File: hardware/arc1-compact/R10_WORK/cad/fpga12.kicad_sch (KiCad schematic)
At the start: 77 parts, among them J10 12F JTAG, U31 LFE5U-12F-6TG144C, U32 iso SCK, U33 iso MOSI, U34 iso SS, U35 iso MISO, X3 25MHz

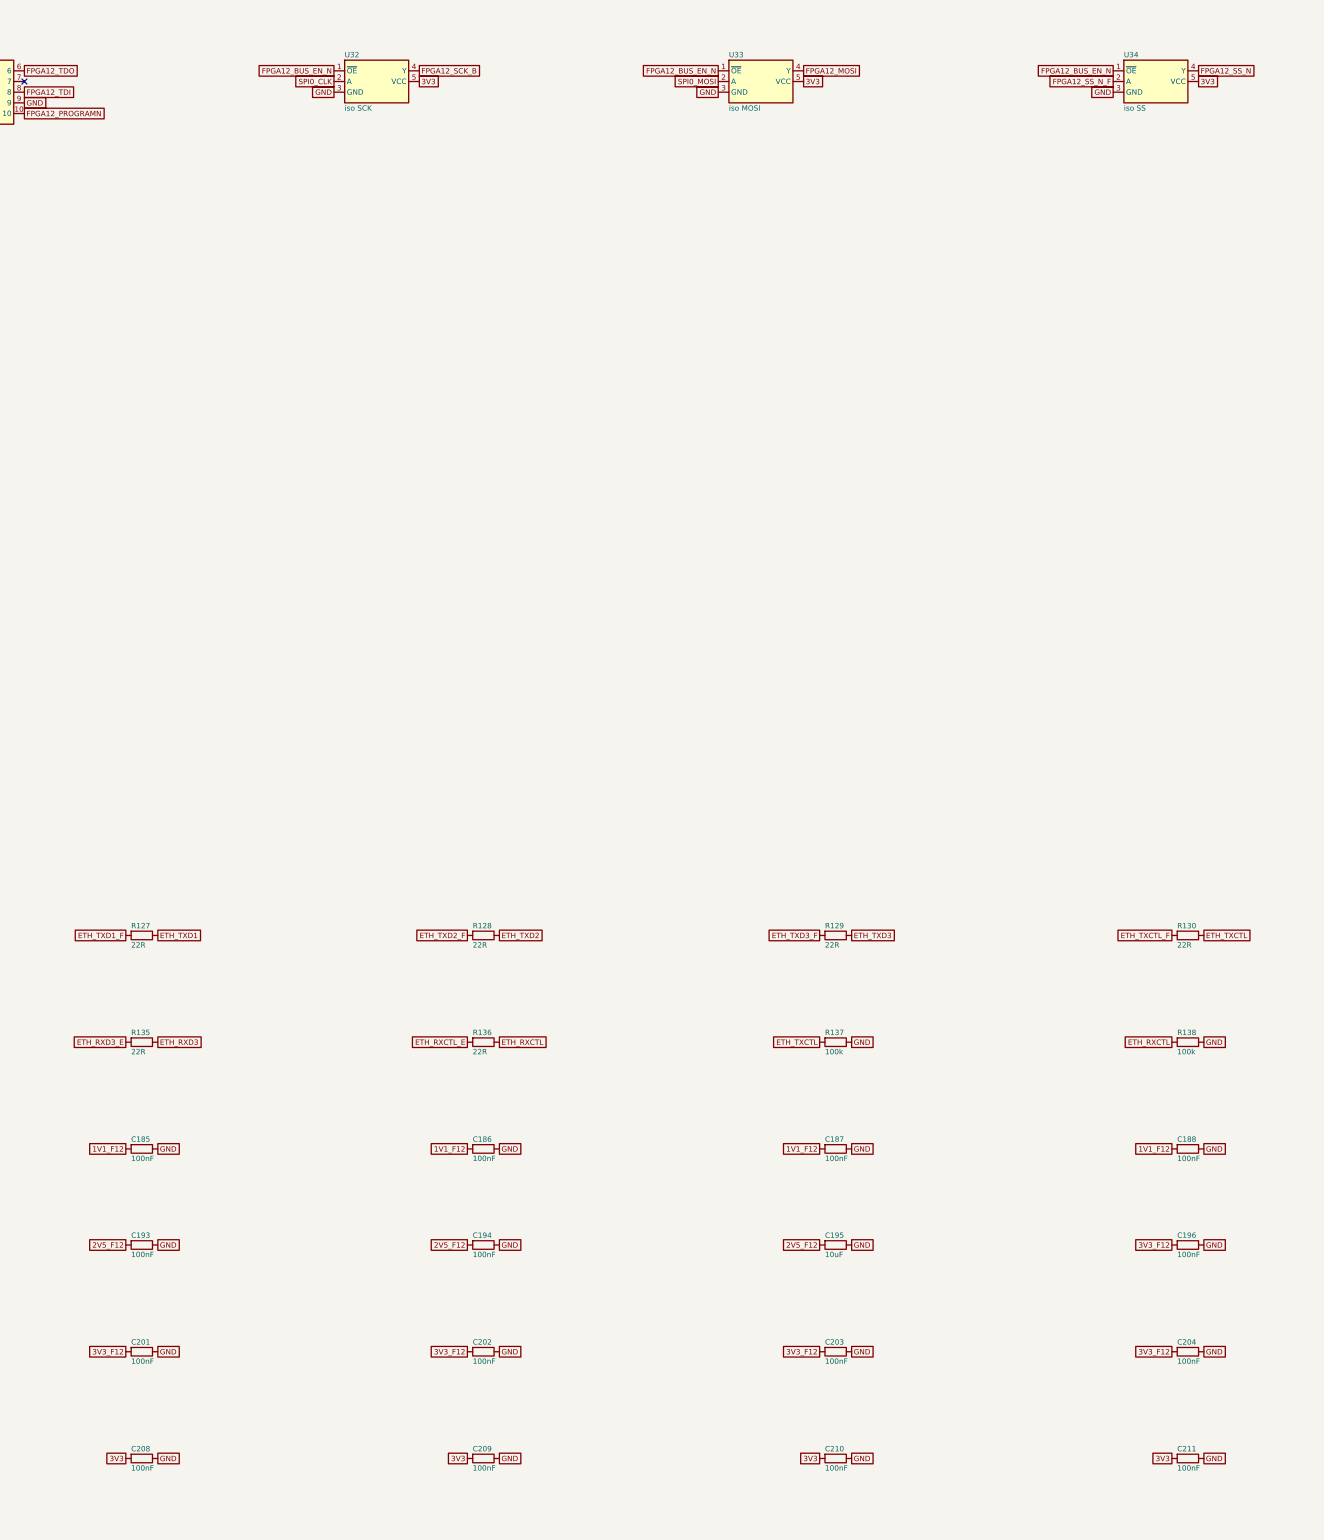
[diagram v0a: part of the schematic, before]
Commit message: R10 schematic: SDRAM net rename (collision with microSD clock found by crosscheck), 12F config buffers on 3V3_F12, crosscheck_r10 (A-H) PASS, every-pin review tables
Co-Authored-By: Claude Opus 5.5 <noreply@anthropic.com>
Claude-Session: https://claude.ai/code/session_01UkiuLdbjDvK75uDzAPKsGs
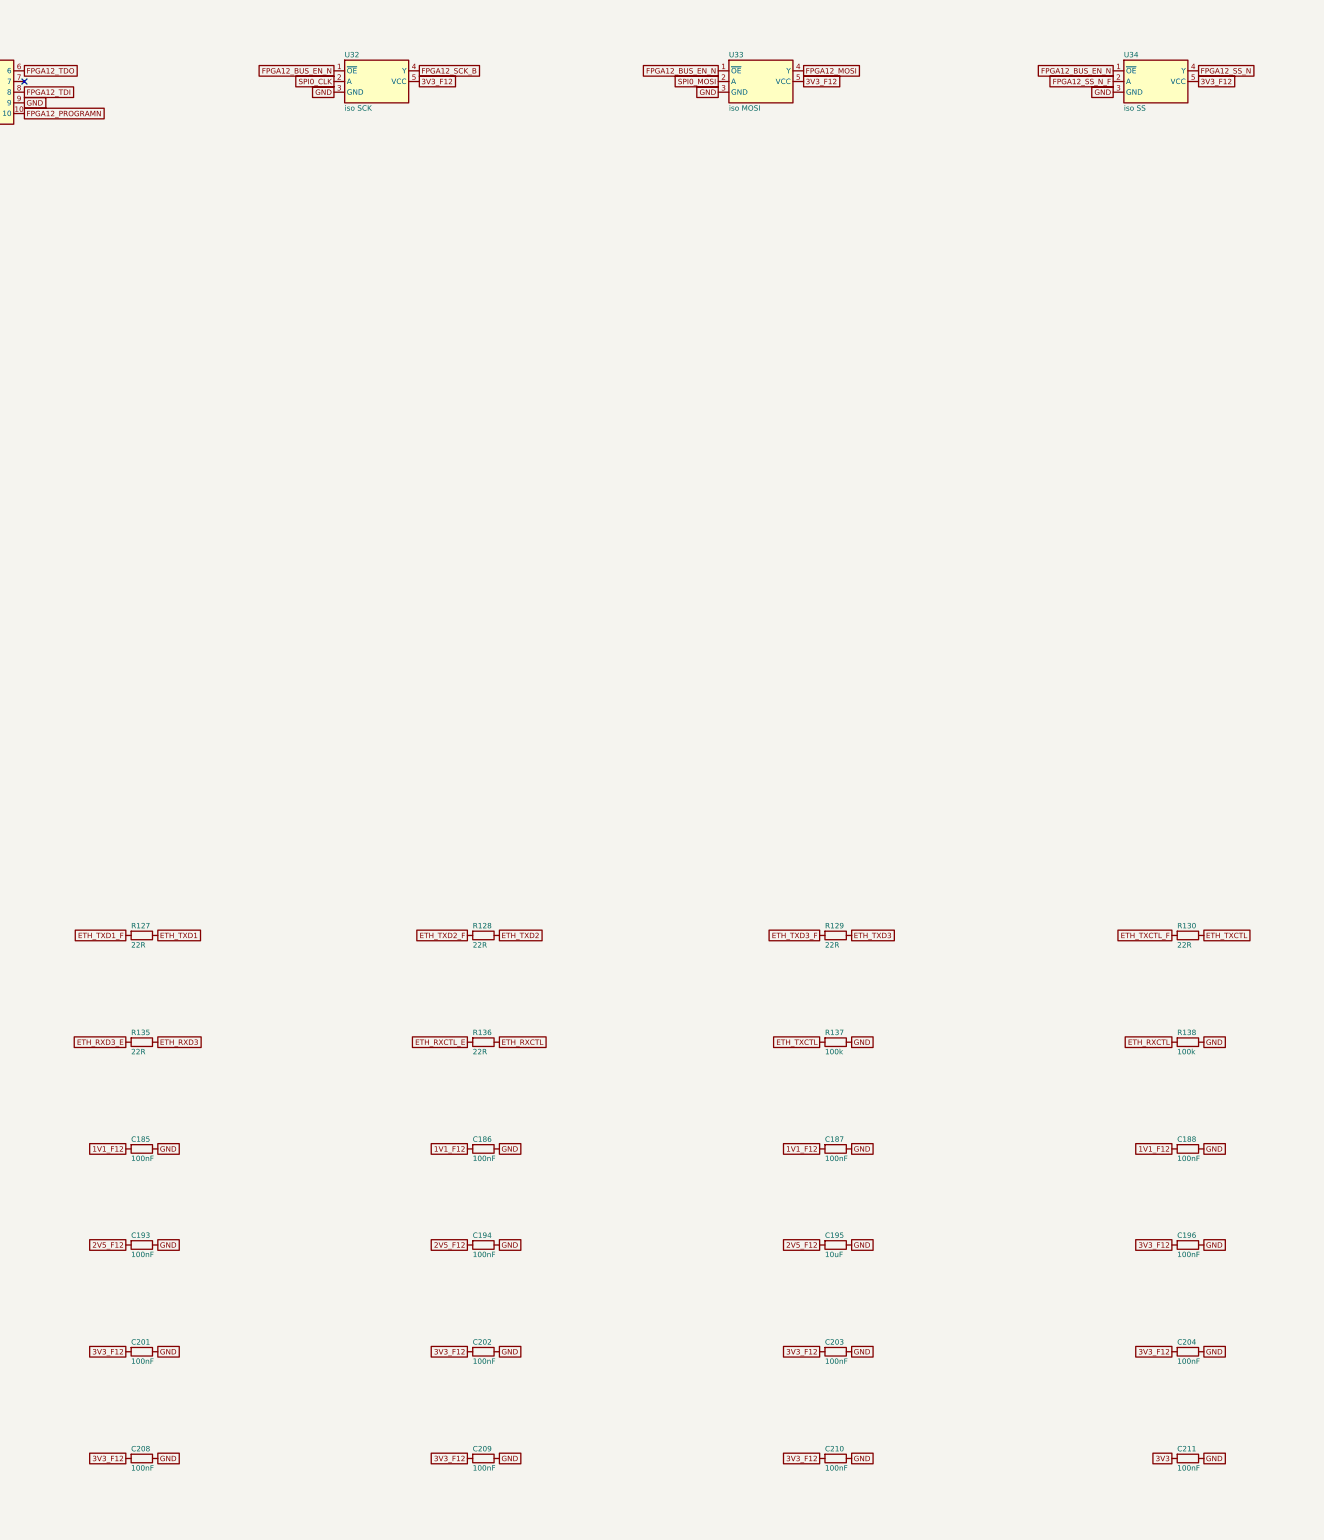
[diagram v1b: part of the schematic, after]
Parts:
- U32, U33, U34: Note (none) -> Ioff: powered with the FPGA it drives
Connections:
- net 3V3: no longer C208.1, C209.1, C210.1, U32.5 (VCC), U33.5 (VCC), U34.5 (VCC)
- net 3V3_F12: now also C208.1, C209.1, C210.1, U32.5 (VCC), U33.5 (VCC), U34.5 (VCC)

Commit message: R10 change order rev 1.1: HDMI audio (ADV7513), USB0 role mux + hub + 2x front USB-A, eMMC, buttonless board
Owner handoff ARC1_R10_Handoff rev 1.1 (spec/, SHA-256 recorded) implemented in the generated schematic:
- D8 ADV7513BSWZ replaces the TFP410 (supersedes D6): D213 RGB888 video, D213 I2C2 init,
  F133 I2S2 -> HDMI embedded audio; own 1.8 V buck + 3 filtered domains; R_EXT 887R.
  D[23:0] pin order verified from the datasheet glyph coordinates.
- D9 F133 USB0 -> TS3USB221A (default rear USB-C device/FEL) or USB2422 hub -> two
  TPS2051C-switched front USB-A ports; F133 USB1 remains the internal D213 link; the D213
  recovery USB-C becomes internal fixture pads.
- D10 Samsung KLMAG1JETD-B041 16 GB eMMC on F133 SMHC0 (CONDITIONAL: SMHC0 documented for SD).
- D11 no switches: fixture pad pairs; game buttons, microSD and speakers removed.
- crosscheck_r10 section I (handoff go/no-go: 4 exterior connectors, 0 switches, I2S wired
  to the HDMI transmitter, USB0/USB1 roles, eMMC wiring) PASS; ERC 0/0; pin review PASS.
Sources: ADV7513 DS Rev B (LCSC copy), ADI AN-1270, Linux adv7511 driver, USB2422
DS00001726A, TPS20xxC SLVSAU6I, Samsung eMMC DS (not committed: vendor-confidential mark).

Co-Authored-By: Claude Opus 5.5 <noreply@anthropic.com>
Claude-Session: https://claude.ai/code/session_01UkiuLdbjDvK75uDzAPKsGs
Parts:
- removed C183, C184, C185, C186, C187, C188, C191, C192, C193, C194, C196, C197, C198, C199, C200, C201, C202, C203, C204: 100nF, Capacitor_SMD:C_0402_1005Metric, symbol ARC1_R10:C0402
- removed C189, C190, C195: 10uF, Capacitor_SMD:C_0603_1608Metric, symbol ARC1_R10:C0603
- removed D5: 12F LED, LED_SMD:LED_0603_1608Metric, symbol ARC1_R10:LED
- removed J10: 12F JTAG, Connector_PinHeader_1.27mm:PinHeader_2x05_P1.27mm_Vertical_SMD, symbol ARC1_R10:HDR_2x5_127
- removed R125, R126, R127, R128, R129, R130: 22R, Resistor_SMD:R_0402_1005Metric, symbol ARC1_R10:R0402
- removed TP59: ETH_TXCK, TestPoint:TestPoint_Pad_D1.0mm, symbol ARC1_R10:TP
- removed TP60: ETH_RXCK, TestPoint:TestPoint_Pad_D1.0mm, symbol ARC1_R10:TP
- removed TP61: FPGA12_DONE, TestPoint:TestPoint_Pad_D1.0mm, symbol ARC1_R10:TP
- removed TP62: FPGA12_PROGRAMN, TestPoint:TestPoint_Pad_D1.0mm, symbol ARC1_R10:TP
- removed TP63: FPGA12_INITN, TestPoint:TestPoint_Pad_D1.0mm, symbol ARC1_R10:TP
- removed TP64: FPGA12_SCK, TestPoint:TestPoint_Pad_D1.0mm, symbol ARC1_R10:TP
- removed U31: LFE5U-12F-6TG144C, Package_QFP:TQFP-144_20x20mm_P0.5mm, symbol ARC1_R10:ECP5_12F_TQ144
- removed U32: iso SCK, Package_TO_SOT_SMD:SOT-353_SC-70-5, symbol ARC1_R10:LVC1G125
- removed U33: iso MOSI, Package_TO_SOT_SMD:SOT-353_SC-70-5, symbol ARC1_R10:LVC1G125
- removed U34: iso SS, Package_TO_SOT_SMD:SOT-353_SC-70-5, symbol ARC1_R10:LVC1G125
- removed U35: iso MISO, Package_TO_SOT_SMD:SOT-353_SC-70-5, symbol ARC1_R10:LVC1G125
- removed X3: 25MHz, Oscillator:Oscillator_SMD_Abracon_ASE-4Pin_3.2x2.5mm, symbol ARC1_R10:OSC_3225
- added C213, C214, C215, C216, C218, C219, C220, C221, C222, C223, C224, C225, C226, C230, C231, C232, C233, C234: 100nF, Capacitor_SMD:C_0402_1005Metric, symbol ARC1_R10:C0402
- added C217, C227, C228, C229: 10uF, Capacitor_SMD:C_0603_1608Metric, symbol ARC1_R10:C0603
- added D6: 12F LED, LED_SMD:LED_0603_1608Metric, symbol ARC1_R10:LED
- added J16: 12F JTAG, Connector_PinHeader_1.27mm:PinHeader_2x05_P1.27mm_Vertical_SMD, symbol ARC1_R10:HDR_2x5_127
- added R158, R159, R160, R161: 4.7k, Resistor_SMD:R_0402_1005Metric, symbol ARC1_R10:R0402
- added R162: 33R, Resistor_SMD:R_0402_1005Metric, symbol ARC1_R10:R0402
- added R163: 1k, Resistor_SMD:R_0402_1005Metric, symbol ARC1_R10:R0402
- added TP67: ETH_TXCK, TestPoint:TestPoint_Pad_D1.0mm, symbol ARC1_R10:TP
- added TP68: ETH_RXCK, TestPoint:TestPoint_Pad_D1.0mm, symbol ARC1_R10:TP
- added TP69: FPGA12_DONE, TestPoint:TestPoint_Pad_D1.0mm, symbol ARC1_R10:TP
- added TP70: FPGA12_PROGRAMN, TestPoint:TestPoint_Pad_D1.0mm, symbol ARC1_R10:TP
- added TP71: FPGA12_INITN, TestPoint:TestPoint_Pad_D1.0mm, symbol ARC1_R10:TP
- added TP72: FPGA12_SCK, TestPoint:TestPoint_Pad_D1.0mm, symbol ARC1_R10:TP
- added U38: LFE5U-12F-6TG144C, Package_QFP:TQFP-144_20x20mm_P0.5mm, symbol ARC1_R10:ECP5_12F_TQ144
- added U39: iso SCK, Package_TO_SOT_SMD:SOT-353_SC-70-5, symbol ARC1_R10:LVC1G125
- added U40: iso MOSI, Package_TO_SOT_SMD:SOT-353_SC-70-5, symbol ARC1_R10:LVC1G125
- added U41: iso SS, Package_TO_SOT_SMD:SOT-353_SC-70-5, symbol ARC1_R10:LVC1G125
- added U42: iso MISO, Package_TO_SOT_SMD:SOT-353_SC-70-5, symbol ARC1_R10:LVC1G125
- added X4: 25MHz, Oscillator:Oscillator_SMD_Abracon_ASE-4Pin_3.2x2.5mm, symbol ARC1_R10:OSC_3225
- C205, C206, C207: value 10uF -> 100nF; footprint Capacitor_SMD:C_0603_1608Metric -> Capacitor_SMD:C_0402_1005Metric; symbol ARC1_R10:C0603 -> ARC1_R10:C0402; LCSC C19702 -> C1525; MPN CL10A106KP8NNNC -> CL05B104KO5NNNC
- C211, C212: value 100nF -> 10uF; footprint Capacitor_SMD:C_0402_1005Metric -> Capacitor_SMD:C_0603_1608Metric; symbol ARC1_R10:C0402 -> ARC1_R10:C0603; LCSC C1525 -> C19702; MPN CL05B104KO5NNNC -> CL10A106KP8NNNC
- R131: Note 12F->F133 series R at the 12F (RXCK) -> F133->12F series R at the F133 (TXCK)
- R132: Note 12F->F133 series R at the 12F (RXD0) -> F133->12F series R at the F133 (TXD0)
- R133: Note 12F->F133 series R at the 12F (RXD1) -> F133->12F series R at the F133 (TXD1)
- R134: Note 12F->F133 series R at the 12F (RXD2) -> F133->12F series R at the F133 (TXD2)
- R135: Note 12F->F133 series R at the 12F (RXD3) -> F133->12F series R at the F133 (TXD3)
- R136: Note 12F->F133 series R at the 12F (RXCTL) -> F133->12F series R at the F133 (TXCTL)
- R137: value 100k -> 22R; LCSC C25741 -> C25092; MPN 0402WGF1003TCE -> 0402WGF220JTCE; Note 12F RX idle while F133 PG12 is hi-Z -> 12F->F133 series R at the 12F (RXCK)
- R138: value 100k -> 22R; LCSC C25741 -> C25092; MPN 0402WGF1003TCE -> 0402WGF220JTCE; Note F133 EMAC RX idle while the 12F is off/unconfigured -> 12F->F133 series R at the 12F (RXD0)
- R139: value 33R -> 22R; LCSC C25105 -> C25092; MPN 0402WGF330JTCE -> 0402WGF220JTCE; Note CCLK series R -> 12F->F133 series R at the 12F (RXD1)
- R140: value 10k -> 22R; LCSC C25744 -> C25092; MPN 0402WGF1002TCE -> 0402WGF220JTCE; Note buffers disabled at reset -> 12F->F133 series R at the 12F (RXD2)
- R141: value 10k -> 22R; LCSC C25744 -> C25092; MPN 0402WGF1002TCE -> 0402WGF220JTCE; Note FPGA deselected, MISO buffer off at reset -> 12F->F133 series R at the 12F (RXD3)
- R142: value 100k -> 22R; LCSC C25741 -> C25092; MPN 0402WGF1003TCE -> 0402WGF220JTCE; Note (none) -> 12F->F133 series R at the 12F (RXCTL)
- R143: Note (none) -> 12F RX idle while F133 PG12 is hi-Z
- R144: value 4.7k -> 100k; LCSC C25900 -> C25741; MPN 0402WGF4701TCE -> 0402WGF1003TCE; Note (none) -> F133 EMAC RX idle while the 12F is off/unconfigured
- R145: value 470R -> 33R; LCSC (none) -> C25105; MPN (none) -> 0402WGF330JTCE; Manufacturer (none) -> UNI-ROYAL; Note F133 PE8 open-drain use -> CCLK series R; Reuse (none) -> SLIM4_R26_BOM_LINE (re-validate)
- R146: value 4.7k -> 10k; LCSC C25900 -> C25744; MPN 0402WGF4701TCE -> 0402WGF1002TCE; Note (none) -> buffers disabled at reset
- R147: value 4.7k -> 10k; LCSC C25900 -> C25744; MPN 0402WGF4701TCE -> 0402WGF1002TCE; Note (none) -> FPGA deselected, MISO buffer off at reset
- R148: value 4.7k -> 100k; LCSC C25900 -> C25741; MPN 0402WGF4701TCE -> 0402WGF1003TCE
- R149: value 4.7k -> 100k; LCSC C25900 -> C25741; MPN 0402WGF4701TCE -> 0402WGF1003TCE; Note CFG[2:0] = 001 slave SPI -> (none)
- R150, R157: value 1k -> 4.7k; LCSC C11702 -> C25900; MPN 0402WGF1001TCE -> 0402WGF4701TCE
- R151: value 4.7k -> 470R; LCSC C25900 -> (none); MPN 0402WGF4701TCE -> (none); Manufacturer UNI-ROYAL -> (none); Note (none) -> F133 PE8 open-drain use; Reuse SLIM4_R26_BOM_LINE (re-validate) -> (none)
- R155: Note open drain to F133 PE5 -> CFG[2:0] = 001 slave SPI
- R156: value 33R -> 1k; LCSC C25105 -> C11702; MPN 0402WGF330JTCE -> 0402WGF1001TCE
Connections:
- net 1V1_F12: now also C205.1, C206.1, C207.1, C208.1, C209.1, C210.1, C211.1, C212.1, U38.130 (VCC), U38.20 (VCC), U38.29 (VCC), U38.38 (VCC), U38.66 (VCC), U38.83 (VCC)
- net 2V5_F12: now also C213.1, C214.1, C215.1, C216.1, C217.1, U38.132 (VCCAUX), U38.17 (VCCAUX), U38.53 (VCCAUX), U38.96 (VCCAUX)
- net 3V3: now also R146.2, R147.2, C233.1, U42.5 (VCC); no longer C211.1, R140.2, R141.2
- net 3V3_F12: now also R156.2, C218.1, C219.1, C220.1, C221.1, C222.1, C223.1, C224.1, C225.1, C226.1, C227.1, C228.1, C229.1, C230.1, C231.1, C232.1, C234.1, J16.1, R158.2, R159.2, R160.2, R161.2, U38.100 (VCCIO2), U38.122 (VCCIO1), U38.137 (VCCIO0), U38.16 (VCCIO6), U38.36 (VCCIO6), U38.43 (VCCIO8), U38.70 (VCCIO3), U38.86 (VCCIO3), U38.9 (VCCIO7), U39.5 (VCC), U40.5 (VCC), U41.5 (VCC), X4.4 (VDD); no longer C205.1, C206.1, C207.1, C208.1, C209.1, C210.1, C212.1, R144.2, R146.2, R147.2, R148.2, R149.2
- net ETH_RXCK: now also R137.2, TP68.1; no longer R131.2
- net ETH_RXCK_E: now also R137.1, U38.110 (PT67A); no longer R131.1
- net ETH_RXCTL: now also R142.2, R144.1; no longer R136.2, R138.1
- net ETH_RXCTL_E: now also R142.1, U38.115 (PT58B); no longer R136.1
- net ETH_RXD0: now also R138.2; no longer R132.2
- net ETH_RXD0_E: now also R138.1, U38.111 (PT62B); no longer R132.1
- net ETH_RXD1: now also R139.2; no longer R133.2
- net ETH_RXD1_E: now also R139.1, U38.112 (PT62A); no longer R133.1
- net ETH_RXD2: now also R140.2; no longer R134.2
- net ETH_RXD2_E: now also R140.1, U38.113 (PT60B); no longer R134.1
- net ETH_RXD3: now also R141.2; no longer R135.2
- net ETH_RXD3_E: now also R141.1, U38.114 (PT60A); no longer R135.1
- net ETH_TXCK: now also R131.2, TP67.1, U38.128 (PT29A/PCLKT0_0)
- net ETH_TXCK_F: now also R131.1
- net ETH_TXCTL: now also R136.2, R143.1, U38.139 (PT9B); no longer R137.1
- net ETH_TXCTL_F: now also R136.1
- net ETH_TXD0: now also R132.2, U38.133 (PT15B)
- net ETH_TXD0_F: now also R132.1
- net ETH_TXD1: now also R133.2, U38.134 (PT15A)
- net ETH_TXD1_F: now also R133.1
- net ETH_TXD2: now also R134.2, U38.135 (PT13B)
- net ETH_TXD2_F: now also R134.1
- net ETH_TXD3: now also R135.2, U38.136 (PT13A)
- net ETH_TXD3_F: now also R135.1
- net F12_LED0: now also R163.1, U38.121 (PT51A); no longer R157.1
- net F12_LED0_R: now also D6.2 (A), R163.2; no longer R157.2
- net F12_OSC_25M: now also R162.2, U38.37 (PL47C/LLC_GPLL0T_IN); no longer R156.2
- net F12_OSC_25M_X: now also R162.1, X4.3 (OUT); no longer R156.1
- net FPGA12_BUS_EN_N: now also R146.1, U39.1 (~{OE}), U40.1 (~{OE}), U41.1 (~{OE}); no longer R140.1
- net FPGA12_CFG0: now also R155.1, U38.62 (CFG_0); no longer R149.1
- net FPGA12_DONE: now also R153.1, TP69.1, U38.56 (DONE); no longer R147.1
- net FPGA12_INITN: now also R152.1, TP71.1, U38.55 (INITN); no longer R146.1
- net FPGA12_IRQ_N: now also R161.1, U38.124 (PT42B); no longer R155.1
- net FPGA12_MISO: now also R149.1, U38.46 (PB11A/D1), U42.2 (A); no longer R143.1
- net FPGA12_MOSI: now also R148.1, U38.47 (PB11B/D0), U40.4 (Y); no longer R142.1
- net FPGA12_PROGRAMN: now also R150.1, R151.2, J16.10, TP70.1, U38.57 (PROGRAMN); no longer R144.1, R145.2
- net FPGA12_PROGRAMN_F: now also R151.1; no longer R145.1
- net FPGA12_SCK: now also R145.2, R156.1, TP72.1, U38.54 (CCLK/MCLK); no longer R139.2, R150.1
- net FPGA12_SCK_B: now also R145.1, U39.4 (Y); no longer R139.1
- net FPGA12_SS_N: now also R154.1, U38.48 (PB13A/SN), U41.4 (Y); no longer R148.1
- net FPGA12_SS_N_F: now also R147.1, U41.2 (A), U42.1 (~{OE}); no longer R141.1
- net FPGA12_TCK: now also R157.1, J16.4, U38.63 (TCK); no longer R151.1
- net FPGA12_TDI: now also J16.8, R159.1, U38.61 (TDI); no longer R153.1
- net FPGA12_TDO: now also J16.6, R160.1, U38.60 (TDO); no longer R154.1
- net FPGA12_TMS: now also J16.2, R158.1, U38.64 (TMS); no longer R152.1
- net FPGA12_VCC_PG: now also X4.1 (OE)
- net GND: now also R144.2, R148.2, R149.2, R157.2, C213.2, C214.2, C215.2, C216.2, C217.2, C218.2, C219.2, C220.2, C221.2, C222.2, C223.2, C224.2, C225.2, C226.2, C227.2, C228.2, C229.2, C230.2, C231.2, C232.2, C233.2, C234.2, D6.1 (K), J16.3, J16.5, J16.9, U38.101 (GND), U38.123 (GND), U38.129 (GND), U38.131 (GND), U38.138 (GND), U38.15 (GND), U38.21 (GND), U38.32 (GND), U38.42 (GND), U38.58 (CFG_2), U38.59 (CFG_1), U38.65 (GND), U38.75 (GND), U38.8 (GND), U38.85 (GND), U38.87 (GND), U39.3 (GND), U40.3 (GND), U41.3 (GND), U42.3 (GND), X4.2 (GND); no longer R137.2, R138.2, R142.2, R151.2
- net PSRAM_CE_N: now also U38.72 (PR44C)
- net PSRAM_SCLK_F: now also U38.73 (PR41D)
- net PSRAM_SIO0: now also U38.74 (PR41C)
- net PSRAM_SIO1: now also U38.76 (PR41B)
- net PSRAM_SIO2: now also U38.77 (PR41A)
- net PSRAM_SIO3: now also U38.78 (PR35D)
- net SPI0_CLK: now also U39.2 (A)
- net SPI0_MISO: now also U42.4 (Y)
- net SPI0_MOSI: now also U40.2 (A)
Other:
- moved on the sheet: C205, C206, C207, C208, C209, C210, C211, C212, R131, R132, R133, R134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
